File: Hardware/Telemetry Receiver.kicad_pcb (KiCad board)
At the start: 4 copper layers, 67 x 23.5 mm, 54 parts, among them IC1 RFX2401C, J1 SMA Connector, J2 USB_C_Receptacle_USB2.0, J3 S4B-XH-A-1, U1 LM1117-3.3, U2 USBLC6-2SC6, U3 STM32L4P5RET6, U4 NRF24L01, U5 36103205S, Y1 Crystal(16MHZ)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

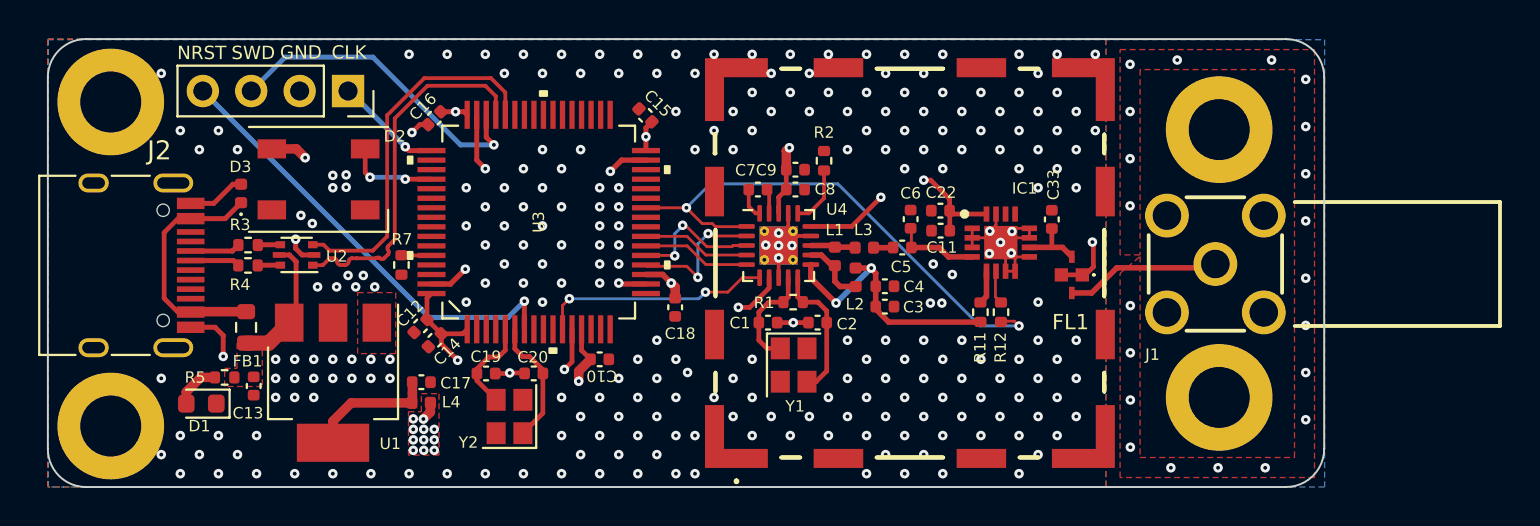
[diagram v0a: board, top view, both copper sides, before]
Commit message: USB C changes
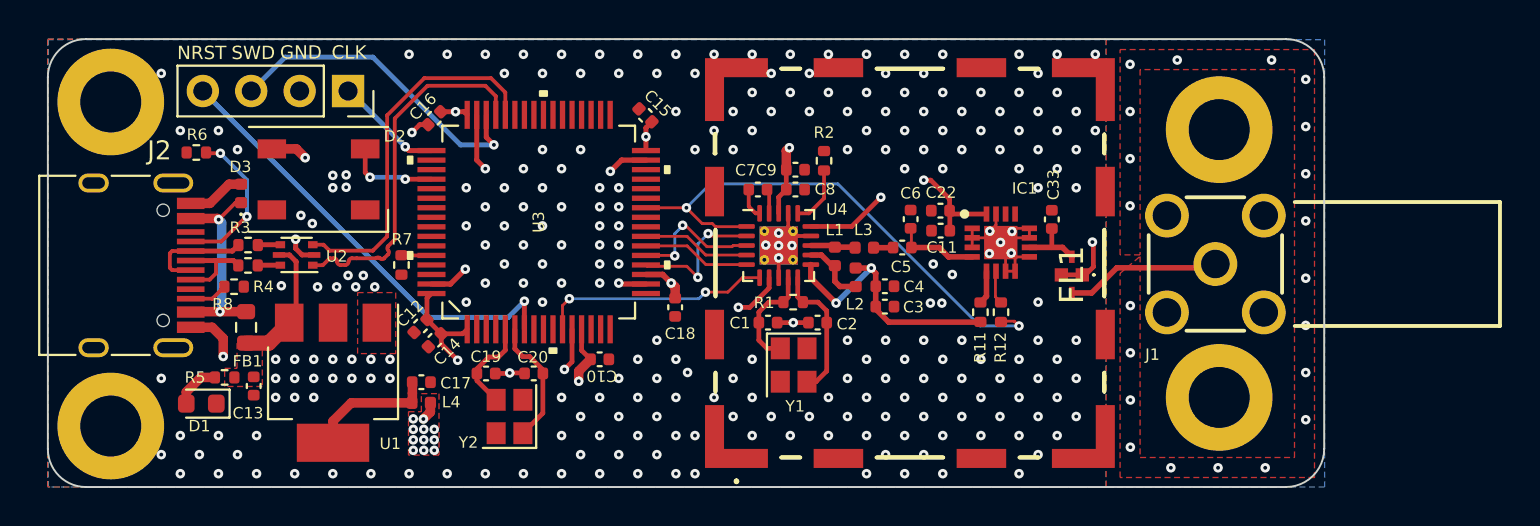
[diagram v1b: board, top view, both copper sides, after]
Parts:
- added R6: 5.1k, Resistor_SMD:R_0402_1005Metric, F.Cu at (88.8, -92.8)
- added R8: 5.1k, Resistor_SMD:R_0402_1005Metric, F.Cu at (90.8, -85.8)
- FL1: footprint footprints:2450BP14D0100T -> Telemetry:2450BP14D0100T
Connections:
- J2 pad A5: unconnected-(J2-PadA5) -> Net-(J2-PadA5)
- J2 pad A7: unconnected-(J2-PadA7) -> /USB_C-
- J2 pad B5: unconnected-(J2-PadB5) -> Net-(J2-PadB5)
- J2 pad B6: unconnected-(J2-PadB6) -> /USB_C+
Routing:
- net Net-(J2-PadA5): track 0.00 -> 8.16 mm, vias 0 -> 2
- net /USB_C-: track 2.13 -> 5.18 mm
- net /USB_C+: track 2.10 -> 4.25 mm
- net Net-(J2-PadB5): track 0.00 -> 2.03 mm
- net GND: track 43.1 -> 44.5 mm
- net Net-(D3-Pad1): track 13.4 -> 12.1 mm, vias 0 -> 2
- removed copper zone on In1.Cu, net GND

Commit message: Signed board
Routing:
- added copper zone on In1.Cu, net GND
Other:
- board text added: "Designed by Adam Wasilewski"
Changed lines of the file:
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@@
   (gr_line (start 81.05 -96.8) (end 81.05 -77.3) (layer "Edge.Cuts") (width 0.1))
   (gr_line (start 146 -98.8) (end 83.05 -98.8) (layer "Edge.Cuts") (width 0.1))
+  (gr_text "Designed by Adam Wasilewski" (at 126.45 -96.15) (layer "B.SilkS")
+    (effects (font (size 1 1) (thickness 0.2)) (justify mirror))
+  )
   (gr_text "NRST\n" (at 89.125 -98.075) (layer "F.SilkS")
     (effects (font (size 0.7 0.7) (thickness 0.1)))
@@
       )
     )
+  )
+  (zone (net 1) (net_name "GND") (layer "In1.Cu") (hatch edge 0.508)
+    (connect_pads yes (clearance 0.508))
+    (min_thickness 0.254) (filled_areas_thickness no)
+    (fill yes (thermal_gap 0.508) (thermal_bridge_width 0.508))
+    (polygon
+      (pts
+        (xy 148.01 -75.31)
+        (xy 81.03 -75.31)
+        (xy 81.029768 -99.010001)
+        (xy 147.949768 -98.700001)
+      )
+    )
